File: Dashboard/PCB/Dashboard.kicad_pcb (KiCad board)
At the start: 4 copper layers, 97.3 x 83.6 mm, 80 parts, among them J1 3.3V step down, J2 5V step down, J3 LED, J4 MAIN_CONNECTOR, J5 BAOFENG_OUT, J6 Display, J7 PROGRAMMER, J8 MEM2051-00-195-00-A_REVC, Q1 BSS138, Q2 BSS138, Q3 BSS138, Q4 BSS138, SW1 SW_SPST, U1 STM32F767ZIT6, U2 MCP2551-I-P, U3 MCP2551-I-P, U4 AS4C1M16S-6TCN, U5 AT25SF128A-SHB-T, Y1 Crystal_GND24

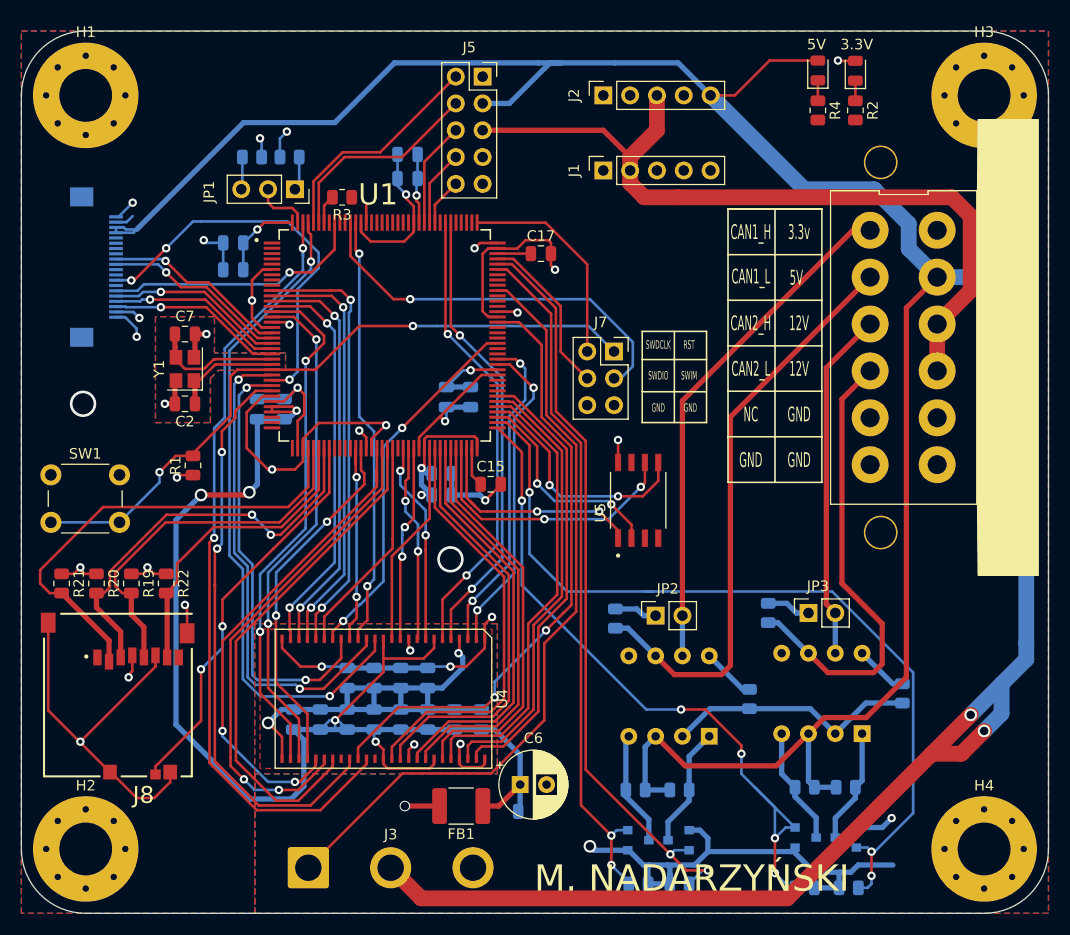
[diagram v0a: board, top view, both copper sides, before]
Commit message: Add buck converter
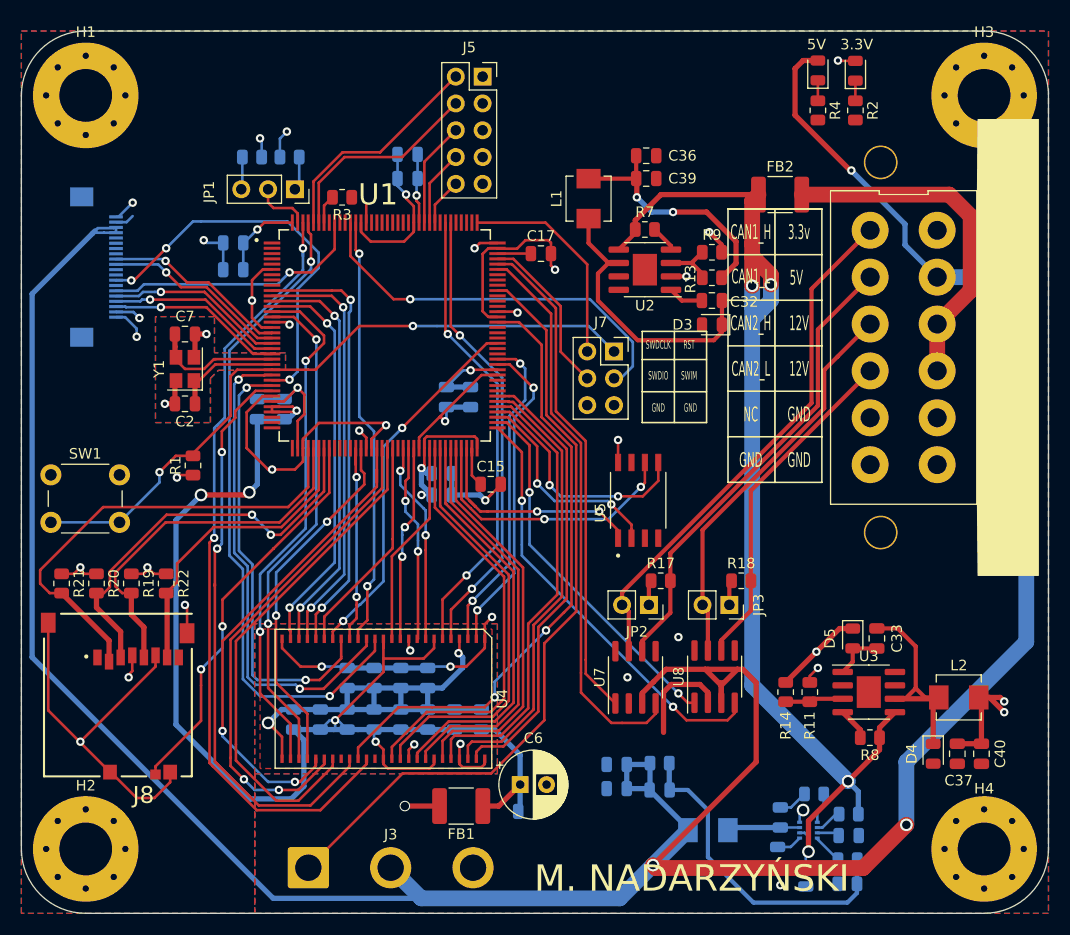
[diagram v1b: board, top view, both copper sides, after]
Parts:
- removed J1: 3.3V step down, Connector_PinSocket_2.54mm:PinSocket_1x05_P2.54mm_Vertical
- removed J2: 5V step down, Connector_PinSocket_2.54mm:PinSocket_1x05_P2.54mm_Vertical
- removed Q1, Q2, Q3, Q4: BSS138, Package_TO_SOT_SMD:SOT-23
- added C16: 100nF, Capacitor_SMD:C_0805_2012Metric, B.Cu at (241.4, 101.2)
- added C18: 1uF, Capacitor_SMD:C_0805_2012Metric, B.Cu at (238.8, 99.3)
- added C31: 1uF, Capacitor_SMD:C_0805_2012Metric, B.Cu at (245.5, 97.3)
- added C32: 10nF, Capacitor_SMD:C_0805_2012Metric, F.Cu at (232.5, 46.6)
- added C33: 10nF, Capacitor_SMD:C_0805_2012Metric, F.Cu at (248.2, 78.6)
- added C34: 1uF, Capacitor_SMD:C_0805_2012Metric, B.Cu at (239.0, 95.6)
- added C35: 10pF, Capacitor_SMD:C_0805_2012Metric, B.Cu at (227.6, 93.0)
- added C36: 10uF, Capacitor_SMD:C_0805_2012Metric, F.Cu at (226.3, 32.9)
- added C37: 10uF, Capacitor_SMD:C_0805_2012Metric, F.Cu at (255.8, 89.5)
- added C38: 22uF, Capacitor_SMD:C_0805_2012Metric, B.Cu at (223.5, 92.8)
- added C39: 10uF, Capacitor_SMD:C_0805_2012Metric, F.Cu at (226.3, 35.1)
- added C40: 10uF, Capacitor_SMD:C_0805_2012Metric, F.Cu at (258.1, 89.5)
- added C41: 22uF, Capacitor_SMD:C_0805_2012Metric, B.Cu at (223.5, 90.6)
- added D3: D_Schottky, Diode_SMD:D_0805_2012Metric, F.Cu at (232.5, 48.9)
- added D4: D_Schottky, Diode_SMD:D_0805_2012Metric, F.Cu at (253.5, 89.5)
- added D5: 1N4148, Diode_SMD:D_0805_2012Metric, F.Cu at (245.9, 78.6)
- added FB2: Ferrite_Bead, Capacitor_SMD:C_1812_4532Metric, F.Cu at (239.0, 36.6)
- added L1: 10uH, Inductor_SMD:L_Vishay_IHLP-1616, F.Cu at (220.9, 37.0)
- added L2: 10uH, Inductor_SMD:L_Vishay_IHLP-1616, F.Cu at (255.9, 84.2)
- added L3: 2.2uH, Inductor_SMD:L_Vishay_IHLP-1616, B.Cu at (232.2, 96.8)
- added R23: 40.2k, Resistor_SMD:R_0805_2012Metric, B.Cu at (227.6, 90.4)
- added U6: MP2332H, SOT-583:SOTFL50P160X60-8N, B.Cu at (241.7, 96.8)
- added U7: MCP2561-E-SN, Package_SO:SOIC-8_3.9x4.9mm_P1.27mm, F.Cu at (225.3, 82.3)
- added U8: MCP2561-E-SN, Package_SO:SOIC-8_3.9x4.9mm_P1.27mm, F.Cu at (232.8, 82.2)
- R11, R13, R14, R9: value 10k -> R; moved to F.Cu
- R12: value 10k -> R
- R15: value 10k -> 20k
- R16: value 10k -> 13k
- R17, R18: moved to F.Cu
- R6: value 10k -> 100k
- R7, R8: value 10k -> 100k; moved to F.Cu
- U2, U3: value MCP2551-I-P -> MP2359DJ-LF-Z; footprint Package_DIP:DIP-8_W7.62mm -> Package_SO:SOIC-8-1EP_3.9x4.9mm_P1.27mm_EP2.29x3mm; moved to F.Cu
- moved R7 62.0 mm to (226.2, 39.9), turned to 0 degrees
- moved R9 60.8 mm to (232.5, 42.0), turned to 0 degrees
- moved R13 49.9 mm to (232.5, 44.5)
- moved U2 44.6 mm to (226.2, 43.7), turned to 180 degrees
- moved R16 19.8 mm to (245.4, 101.9), turned to 180 degrees
- moved R6 17.3 mm to (245.5, 95.2), turned to 180 degrees
- moved R12 16.9 mm to (242.2, 93.3), turned to 0 degrees
- moved R15 16.6 mm to (245.4, 99.6), turned to 180 degrees
- moved R11 15.4 mm to (241.8, 83.7), turned to 90 degrees
- moved R8 14.4 mm to (247.5, 88.0), turned to 180 degrees
- moved R14 9.20 mm to (239.5, 83.7), turned to 90 degrees
- moved JP3 7.53 mm to (234.2, 75.4), turned to 270 degrees
- moved R17 5.59 mm to (227.7, 73.2), turned to 0 degrees
- moved U3 3.99 mm to (247.4, 83.7), turned to 0 degrees
- moved R18 3.98 mm to (235.3, 73.2), turned to 0 degrees
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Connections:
- R11 pad 1: +5V -> Net-(R11-Pad1)
- R11 pad 2: Net-(Q1-Pad3) -> GND
- R12 pad 1: +5V -> Net-(C34-Pad1)
- R12 pad 2: Net-(Q2-Pad3) -> Net-(R12-Pad2)
- R13 pad 1: +5V -> Net-(R13-Pad1)
- R13 pad 2: Net-(Q3-Pad3) -> +8V
- R14 pad 1: +5V -> Net-(R11-Pad1)
- R14 pad 2: Net-(Q4-Pad3) -> +3V3
- R15 pad 1: GND -> Net-(C35-Pad1)
- R16 pad 1: GND -> Net-(C35-Pad1)
- R16 pad 2: Net-(R16-Pad2) -> GND
- R6 pad 1: +3V3 -> +12L
- R6 pad 2: CAN_1_1 -> Net-(R6-Pad2)
- R7 pad 1: +3V3 -> +12L
- R7 pad 2: CAN_1_2 -> Net-(R7-Pad2)
- R8 pad 1: +3V3 -> +12L
- R8 pad 2: CAN_2_1 -> Net-(R8-Pad2)
- R9 pad 1: +3V3 -> Net-(R13-Pad1)
- R9 pad 2: CAN_2_2 -> GND
- U2 pad 1: Net-(Q1-Pad3) -> Net-(C32-Pad1)
- U2 pad 3: +5V -> Net-(R13-Pad1)
- U2 pad 4: Net-(Q2-Pad3) -> Net-(R7-Pad2)
- U2 pad 5: Net-(U2-Pad5) -> +12L
- U2 pad 6: CAN_L1 -> Net-(C32-Pad2)
- U2 pad 7: CAN_H1 -> (no net)
- U2 pad 8: Net-(R16-Pad2) -> (no net)
- U3 pad 1: Net-(Q3-Pad3) -> Net-(C33-Pad1)
- U3 pad 3: +5V -> Net-(R11-Pad1)
- U3 pad 4: Net-(Q4-Pad3) -> Net-(R8-Pad2)
- U3 pad 5: Net-(U3-Pad5) -> +12L
- U3 pad 6: CAN_L2 -> Net-(C33-Pad2)
- U3 pad 7: CAN_H2 -> (no net)
- U3 pad 8: Net-(R15-Pad2) -> (no net)
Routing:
- net +12L: track 0.00 -> 107.1 mm, vias 0 -> 4
- net CAN_2_1: track 80.8 -> 35.2 mm, vias 3 -> 2
- net +12V: track 73.9 -> 32.8 mm
- net Net-(C35-Pad1): track 0.00 -> 33.2 mm
- net +3V3: track 192.5 -> 162.5 mm, vias 24 -> 25
- net Net-(C32-Pad2): track 0.00 -> 26.5 mm
- net CAN_2_2: track 66.5 -> 40.9 mm, vias 5 -> 2
- net CAN_1_1: track 71.9 -> 47.0 mm, vias 2 -> 0
- net +5V: track 323.2 -> 298.6 mm, vias 2 -> 3
- net +8V: track 0.00 -> 23.6 mm, vias 0 -> 2
- net Net-(C33-Pad2): track 0.00 -> 22.1 mm
- net CAN_1_2: track 65.6 -> 53.5 mm, vias 2 -> 0
- net Net-(Q1-Pad3): track 11.5 -> 0.00 mm
- net CAN_L2: track 43.5 -> 32.3 mm
- net Net-(Q4-Pad3): track 11.2 -> 0.00 mm
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
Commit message: Remove unnecessary files
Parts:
- removed J5: BAOFENG_OUT, Connector_PinSocket_2.54mm:PinSocket_2x05_P2.54mm_Vertical
- moved J4 59.1 mm to (198.2, 23.9), turned to 0 degrees
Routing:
- net BAOFENG_OUT_5: track 21.5 -> 0.00 mm
- net BAOFENG_OUT_4: track 19.9 -> 0.00 mm
- net BAOFENG_OUT_3: track 9.99 -> 0.00 mm
- net BAOFENG_OUT_2: track 7.24 -> 0.00 mm
- net BAOFENG_OUT_1: track 4.49 -> 0.00 mm
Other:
- board size 97.3 x 83.6 mm -> 97.3 x 90.3 mm

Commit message: ADD new pcb files
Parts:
- removed G***: LOGO, PGR_logo:logo
- removed J4: MAIN_CONNECTOR, Connector:DT13
- removed J6: Display, Connector_FFC-FPC:Hirose_FH12-20S-0.5SH_1x20-1MP_P0.50mm_Horizontal
- removed J8: MEM2051-00-195-00-A_REVC, SDCARD:GCT_MEM2051-00-195-00-A_REVC
- removed R22: 47K, Resistor_SMD:R_0805_2012Metric
- added J1: Display, Connector_FFC-FPC:Hirose_FH12-40S-0.5SH_1x40-1MP_P0.50mm_Horizontal, B.Cu at (174.1, 80.5)
- added J2: Conn_01x26_Female, Konektor:64734231, F.Cu at (191.6, 61.4)
- added U10: 24LC01, Package_DIP:DIP-8_W7.62mm_Socket_LongPads, F.Cu at (154.8, 82.6)
- added U9: ESP-12S, ESP-12S:ESP-12S, F.Cu at (131.0, 47.8)
- C1, C10, C11, C12, C13, C14, C16, C18, C19, C20, C21, C22, C23, C24, C25, C26, C27, C28, C29, C3, C30, C31, C34, C35, C38, C4, C41, C5, C8, C9, L3, R10, R12, R15, R16, R23, R5, R6, U6: moved to F.Cu
- R19, R20, R21: value 47K -> 10k
- moved D2 208.3 mm to (129.7, 199.9), turned to 0 degrees
- moved H3 205.5 mm to (53.1, 38.2)
- moved D4 194.6 mm to (72.0, 159.6), turned to 0 degrees
- moved H1 194.0 mm to (45.7, 173.4)
- moved C1 186.1 mm to (67.5, 159.6)
- moved R4 185.8 mm to (146.9, 187.8), turned to 0 degrees
- moved C32 182.1 mm to (129.7, 196.9)
- moved R9 179.6 mm to (138.6, 195.2)
- moved R3 171.7 mm to (138.6, 198.1), turned to 0 degrees
- moved R10 168.3 mm to (185.6, 201.3)
- moved C40 163.6 mm to (134.2, 196.4), turned to 0 degrees
- moved D5 163.0 mm to (93.9, 137.7), turned to 0 degrees
- moved C36 162.4 mm to (189.5, 191.0), turned to 0 degrees
- moved R2 161.0 mm to (204.7, 184.2), turned to 0 degrees
- moved R7 161.0 mm to (191.3, 197.0)
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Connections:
- net BAOFENG_OUT_2 renamed Net-(U1-Pad118)
- net BAOFENG_OUT_3 renamed Net-(U1-Pad119)
- R19 pad 1: +3V3 -> Net-(R19-Pad1)
- R19 pad 2: /SD_SCLK -> Net-(R19-Pad2)
- R20 pad 1: +3V3 -> Net-(R20-Pad1)
- R20 pad 2: /SD_MOSI -> Net-(R20-Pad2)
- R21 pad 1: +3V3 -> GND
- R21 pad 2: /SD_CS -> Net-(R21-Pad2)
- U1 pad 100: Net-(U1-Pad100) -> /I2C3_SCL
- U1 pad 102: Net-(U1-Pad102) -> /LTDC_B1
- U1 pad 113: Net-(U1-Pad113) -> ESP_UART_RX
- U1 pad 116: Net-(U1-Pad116) -> ESP_UART_TX
- U1 pad 117: BAOFENG_OUT_1 -> /LTDC_G7
- U1 pad 122: Net-(U1-Pad122) -> /LTDC_B2
- U1 pad 125: Net-(U1-Pad125) -> /LTDC_G3
- U1 pad 126: Net-(U1-Pad126) -> /LTDC_B3
- U1 pad 127: Net-(U1-Pad127) -> /LTDC_B4
- U1 pad 128: Net-(U1-Pad128) -> /LTDC_R0
- U1 pad 134: Net-(U1-Pad134) -> LED_DATA
- U1 pad 136: /D_QUADSPI_NCS -> /QUADSPI_NCS
- U1 pad 139: BAOFENG_OUT_4 -> /LTDC_B6
- U1 pad 140: BAOFENG_OUT_5 -> /LTDC_B7
- U1 pad 18: /D_QUADSPI_BK1_IO3 -> /QUADSPI_IO3
- U1 pad 19: /D_QUADSPI_BK1_IO2 -> /QUADSPI_IO2
- U1 pad 20: /D_QUADSPI_BK1_IO0 -> /QUADSPI_IO0
- U1 pad 21: /D_QUADSPI_BK1_IO1 -> /QUADSPI_IO1
- U1 pad 22: /D_QUADSPI_CLK -> /LTDC_DE
- U1 pad 26: /FMC_SDNWE -> /LTDC_R5
- U1 pad 27: /D_POWER_DOWN -> Net-(U1-Pad27)
- U1 pad 3: Net-(U1-Pad3) -> /LTDC_B0
- U1 pad 35: Net-(U1-Pad35) -> /LTDC_R2
- U1 pad 36: Net-(U1-Pad36) -> /LTDC_R1
- U1 pad 37: Net-(U1-Pad37) -> /LTDC_B5
- U1 pad 4: Net-(U1-Pad4) -> /LTDC_G0
- U1 pad 40: /SD_CS -> /LTDC_VSYNC
- U1 pad 41: /SD_SCLK -> /LTDC_R4
- U1 pad 42: /SD_MISO -> /LTDC_G2
- U1 pad 43: /SD_MOSI -> /FMC_SDNWE
- U1 pad 46: Net-(U1-Pad46) -> /LTDC_R3
- U1 pad 47: Net-(U1-Pad47) -> /LTDC_R6
- U1 pad 48: Net-(U1-Pad48) -> /QUADSPI_CLK
- U1 pad 5: Net-(U1-Pad5) -> /LTDC_G1
- U1 pad 69: /FLASH_SCK -> /LTDC_G4
- U1 pad 70: /FLASH_CS -> /LTDC_G5
- U1 pad 75: /FLASH_MISO -> Net-(U1-Pad75)
- U1 pad 76: /FLASH_MOSI -> Net-(U1-Pad76)
- U1 pad 91: Net-(U1-Pad91) -> /LTDC_R7
- U1 pad 92: Net-(U1-Pad92) -> /LTDC_CLK
- U1 pad 96: Net-(U1-Pad96) -> /LTDC_HSYNC
- U1 pad 97: Net-(U1-Pad97) -> /LTDC_G6
- U1 pad 99: LED_DATA -> /I2C3_SDA
- U5 pad 1: /FLASH_CS -> /QUADSPI_NCS
- U5 pad 2: /FLASH_MISO -> /QUADSPI_IO1
- U5 pad 3: Net-(U5-Pad3) -> /QUADSPI_IO2
- U5 pad 5: /FLASH_MOSI -> /QUADSPI_IO0
- U5 pad 6: /FLASH_SCK -> /QUADSPI_CLK
- U5 pad 7: Net-(U5-Pad7) -> /QUADSPI_IO3
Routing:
- net +5V: track 298.6 -> 0.00 mm, vias 3 -> 0
- net GND: track 236.8 -> 5.40 mm, vias 27 -> 0
- net +3V3: track 162.5 -> 0.00 mm, vias 25 -> 0
- net +3.3VA: track 128.2 -> 2.10 mm, vias 5 -> 1
- net +12L: track 107.1 -> 0.00 mm, vias 4 -> 0
- net /LTDC_R1: track 0.00 -> 81.2 mm, vias 0 -> 3
- net /LTDC_R3: track 0.00 -> 80.1 mm, vias 0 -> 3
- net /LTDC_R5: track 0.00 -> 80.0 mm, vias 0 -> 5
- net /LTDC_B7: track 0.00 -> 78.8 mm, vias 0 -> 3
- net /LTDC_R6: track 0.00 -> 78.7 mm, vias 0 -> 3
- net /LTDC_R2: track 0.00 -> 78.4 mm, vias 0 -> 3
- net /LTDC_G2: track 0.00 -> 77.3 mm, vias 0 -> 5
- net /LTDC_R0: track 0.00 -> 77.0 mm, vias 0 -> 1
- net /LTDC_G0: track 0.00 -> 76.9 mm, vias 0 -> 1
- net /LTDC_G1: track 0.00 -> 74.3 mm, vias 0 -> 1
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- removed copper zone on In2.Cu, net +3V3
- removed copper zone on B.Cu, net GND
- removed copper zone on F.Cu, net GND
- removed copper zone on In1.Cu, net GND
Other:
- board outline removed
- board text removed: "12V"
- board text removed: "3.3V"
- board text removed: "3.3v"
- board text removed: "5V"
- board text removed: "CAN1_H"
- board text removed: "CAN1_L"
- board text removed: "CAN2_H"
- board text removed: "CAN2_L"
- board text removed: "GND"
- board text removed: "M. NADARZYŃSKI"
- board text removed: "NC"
- board text removed: "RST"
- board text removed: "SWDCLK"
- board text removed: "SWDIO"
- board text removed: "SWIM"
